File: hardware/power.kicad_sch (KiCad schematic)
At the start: 7 parts, among them IC2 UCC33420QRAQRQ1, IC3 ISOUSB111DWR

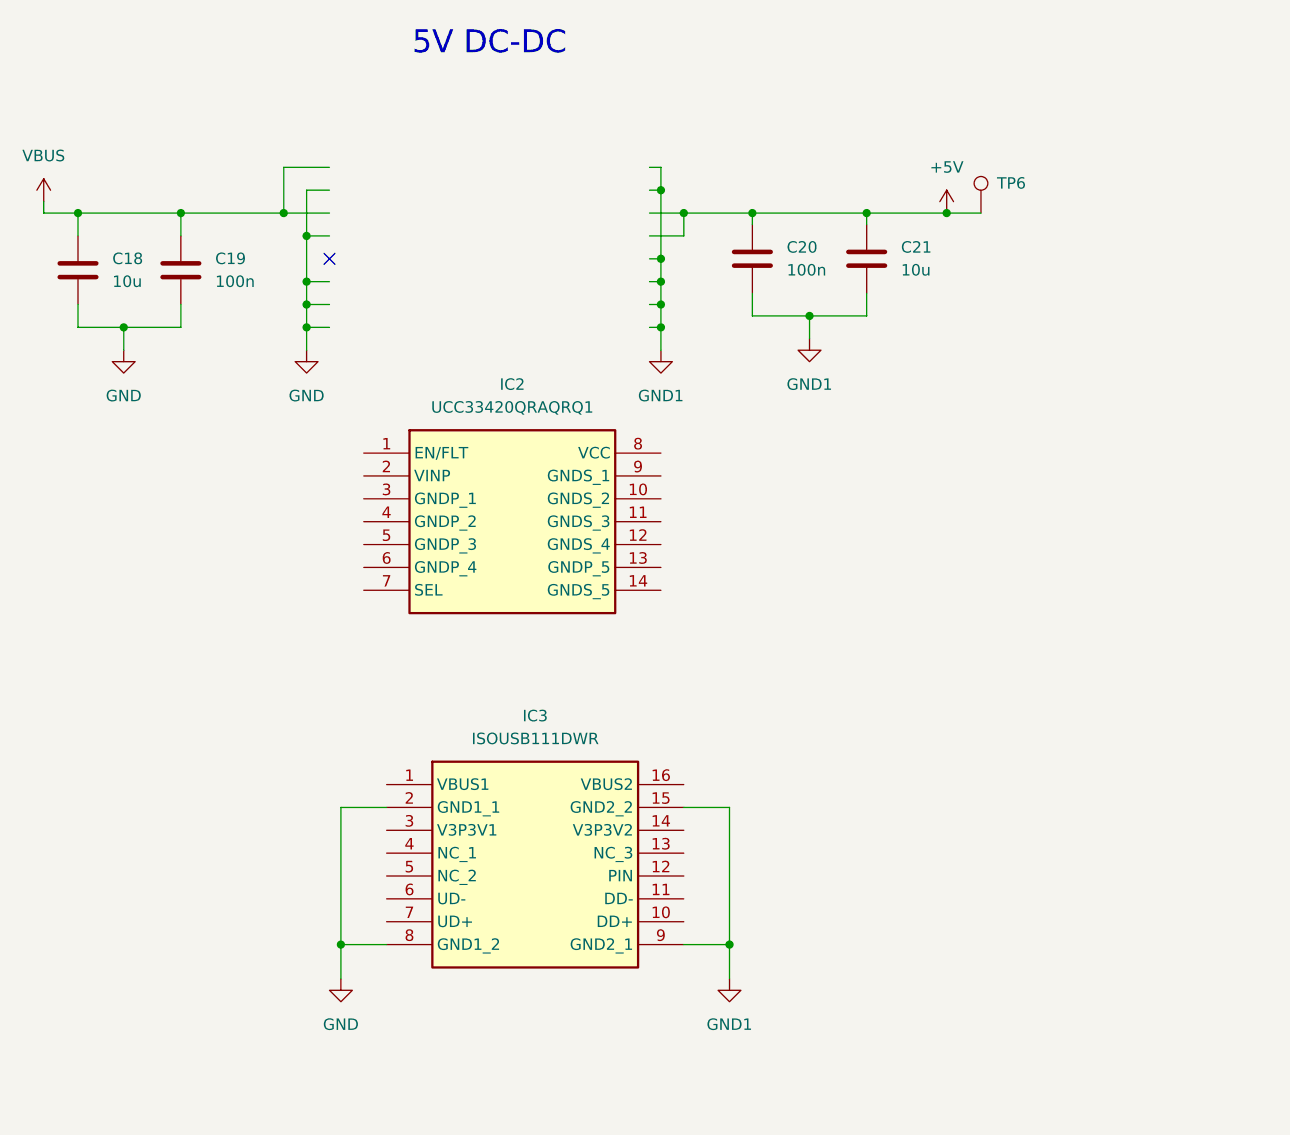
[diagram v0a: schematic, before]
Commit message: Moved GND points, revised DCDC and base USB Work
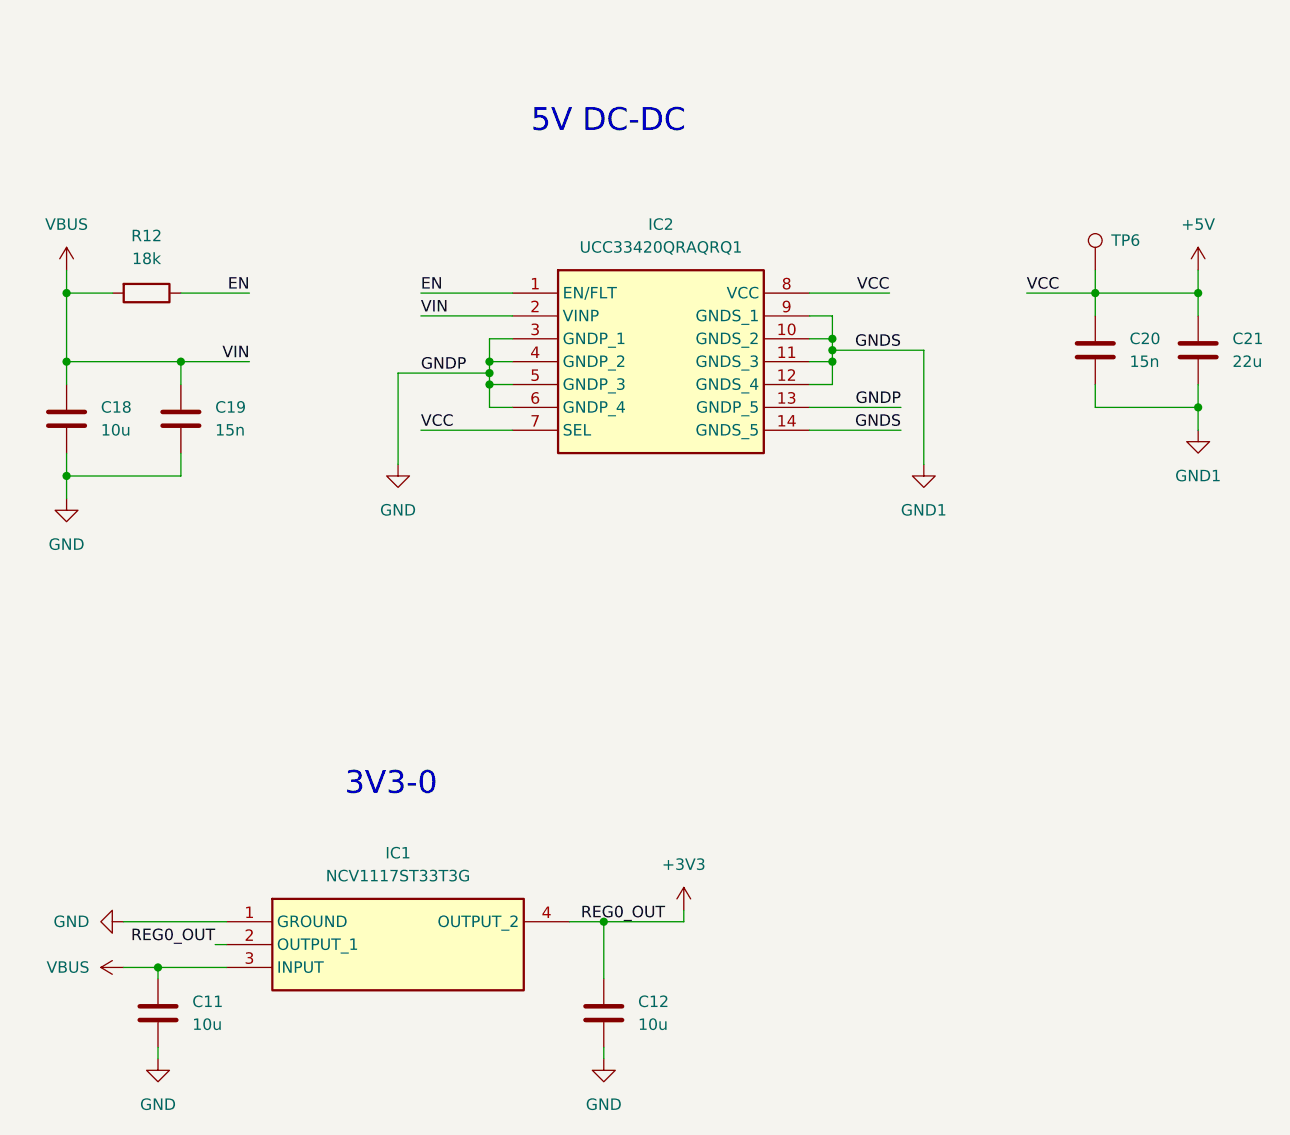
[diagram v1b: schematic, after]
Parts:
- removed IC3: ISOUSB111DWR, Stuttgart:SOIC127P1030X265-16N, symbol Stuttgart:ISOUSB111DWR
- added C11, C12: 10u, Capacitor_SMD:C_0805_2012Metric, symbol Device:C
- added IC1: NCV1117ST33T3G, Stuttgart:SOT230P700X180-4N, symbol Stuttgart:NCV1117ST33T3G
- added R12: 18k, Resistor_SMD:R_0402_1005Metric, symbol Device:R
- C19, C20: value 100n -> 15n; footprint Capacitor_SMD:C_0603_1608Metric -> Capacitor_SMD:C_0402_1005Metric
- C21: value 10u -> 22u
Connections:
- net +5V: now also IC2.7 (SEL), IC2.8 (VCC)
- net GND: now also IC2.13 (GNDP_5), IC2.3 (GNDP_1), IC2.4 (GNDP_2), IC2.5 (GNDP_3), IC2.6 (GNDP_4), C11.2, C12.2, IC1.1 (GROUND)
- net GND1: now also IC2.10 (GNDS_2), IC2.11 (GNDS_3), IC2.12 (GNDS_4), IC2.14 (GNDS_5), IC2.9 (GNDS_1)
- net VBUS: now also IC2.2 (VINP), C11.1, IC1.3 (INPUT), R12.2
- net EN: now reaches IC2.1 (EN/FLT)
- net EN: now also R12.1
- new net +3V3: C12.1, IC1.2 (OUTPUT_1), IC1.4 (OUTPUT_2)
- no-connect marks 1 -> 0
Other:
- note added: "3V3-0"
- moved on the sheet: C18, C19, C20, C21, IC2, TP6

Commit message: Schematic and PCB layout near final
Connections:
- net +5V: now also C11.1, IC1.3 (INPUT)
- net GND: no longer C11.2, C12.2, IC1.1 (GROUND)
- net GND1: now also C11.2, C12.2, IC1.1 (GROUND)
- net VBUS: no longer C11.1, IC1.3 (INPUT)

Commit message: Schematic Clean Up
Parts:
- IC1: JLC Part Number (none) -> C114733
- IC2: JLC Part Number (none) -> C46461551
- TP6: now left out of the parts list
